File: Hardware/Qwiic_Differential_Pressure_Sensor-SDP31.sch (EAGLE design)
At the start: 27 parts, among them J2 QWIIC_RIGHT_ANGLE, J4 QWIIC_RIGHT_ANGLE, U1 SDP31

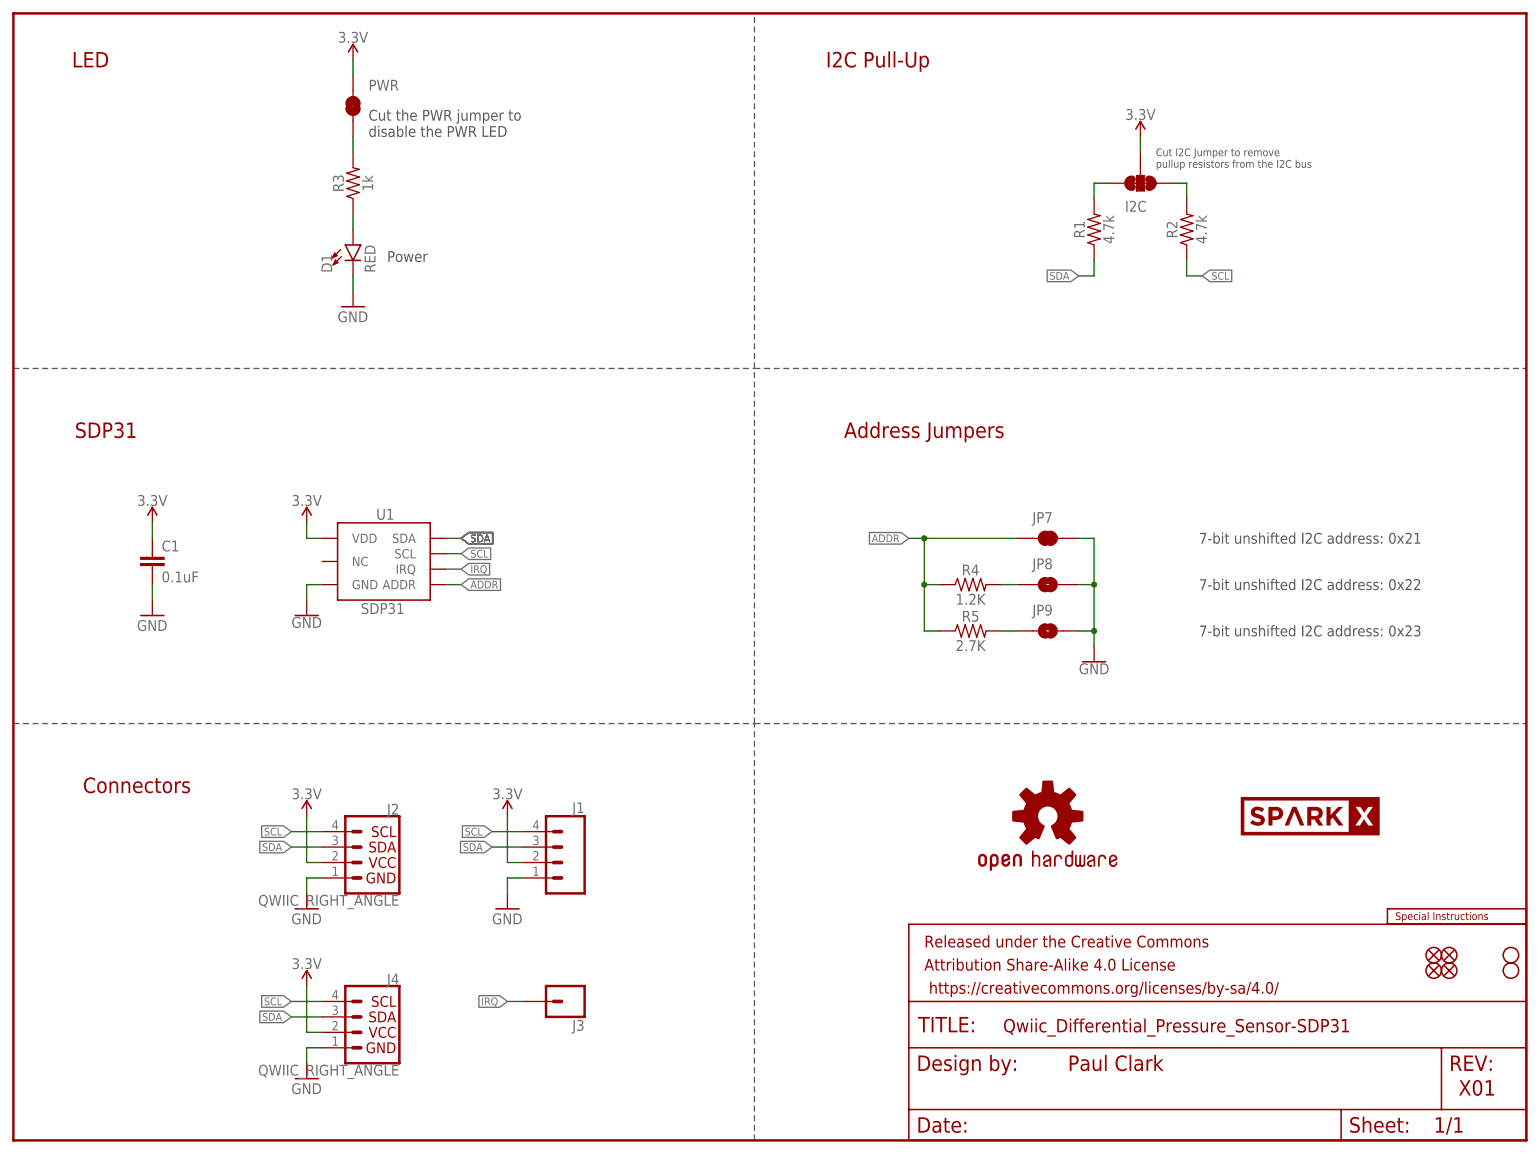
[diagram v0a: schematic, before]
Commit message: Change IRQ to INT. Add Address label.
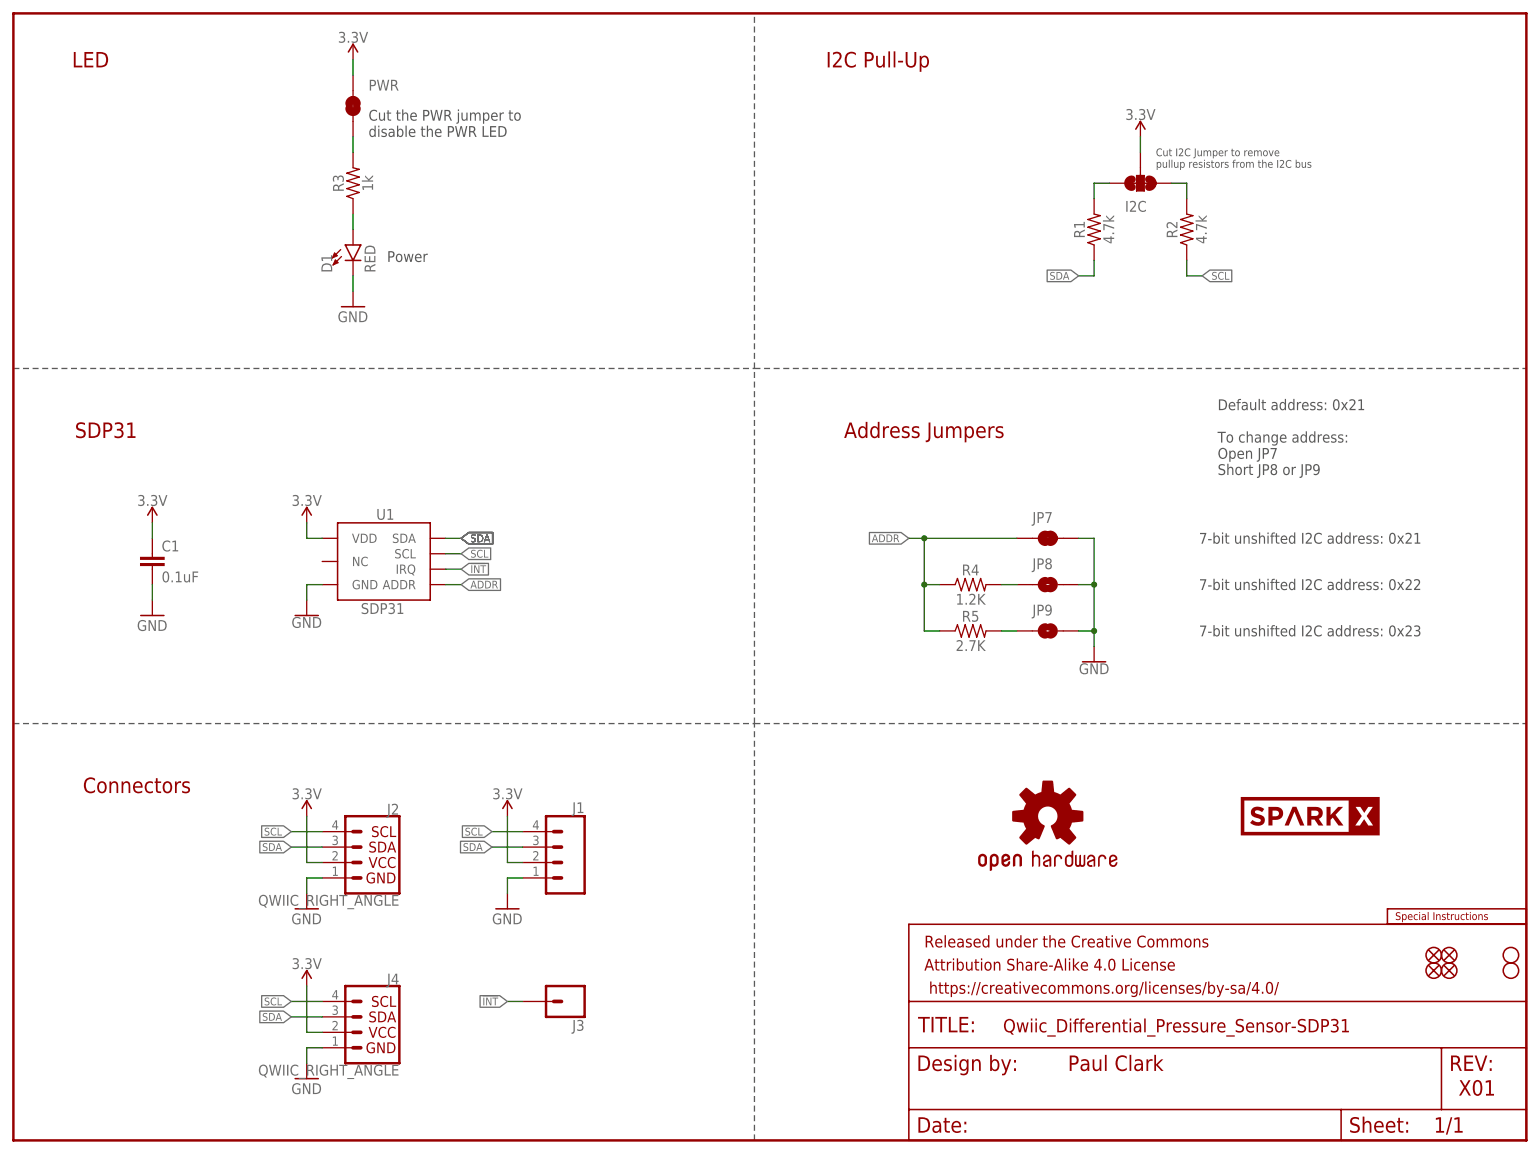
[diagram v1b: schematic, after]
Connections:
- net IRQ renamed !INT!
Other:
- note added: "Default address: 0x21 To change address: Open JP7 Short JP8 or JP9"
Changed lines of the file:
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@@
 <text x="213.36" y="91.44" size="1.778" layer="97" font="vector" align="center">7-bit unshifted I2C address: 0x22</text>
 <text x="213.36" y="83.82" size="1.778" layer="97" font="vector" align="center">7-bit unshifted I2C address: 0x23</text>
+<text x="198.12" y="121.92" size="1.778" layer="97" font="vector" align="top-left">Default address: 0x21
+To change address:
+Open JP7
+Short JP8 or JP9</text>
 </plain>
 <instances>
@@
 </segment>
 </net>
-<net name="IRQ" class="0">
+<net name="!INT!" class="0">
 <segment>
 <pinref part="U1" gate="G$1" pin="IRQ"/>
